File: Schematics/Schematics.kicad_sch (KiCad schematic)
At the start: 19 parts, among them U1 TP4056, U2 BH1750, U3 BME688, U4 BU30TD3WG, U5 NRF52840-DONGLE, U6 LIS3DH

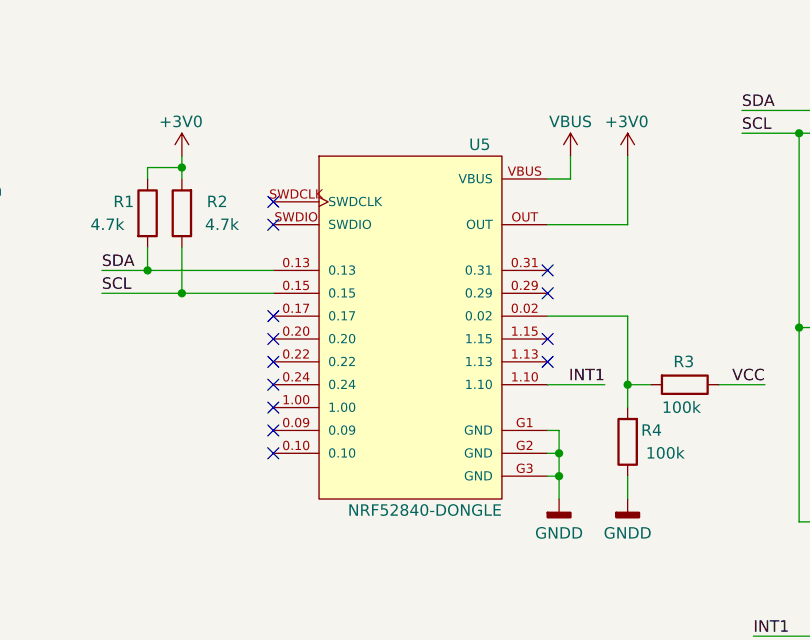
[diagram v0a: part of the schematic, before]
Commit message: Fixed some footprints and made changes on the leader node pcb
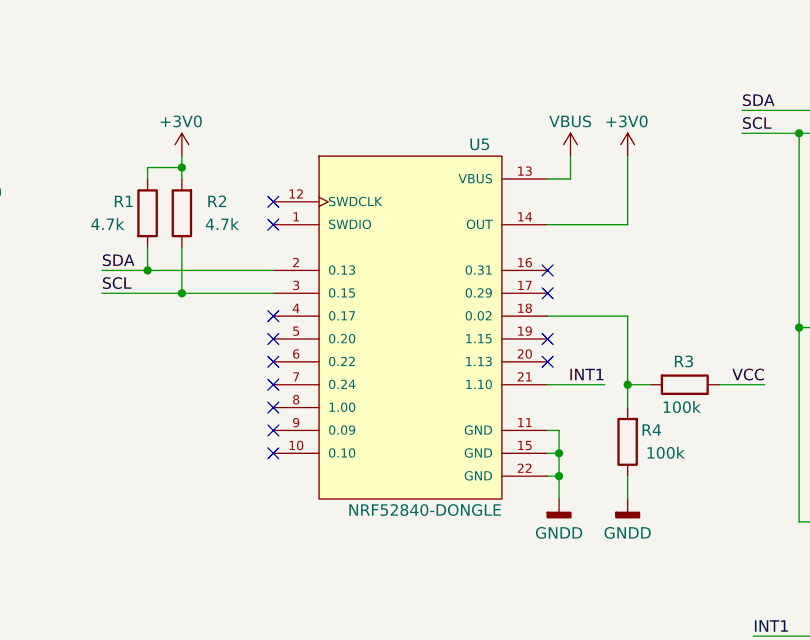
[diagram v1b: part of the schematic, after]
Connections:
- net +3V0: now also U5.14 (OUT); no longer U5.OUT
- net GNDD: now also U5.11 (GND), U5.15 (GND), U5.22 (GND); no longer U5.G1 (GND), U5.G2 (GND), U5.G3 (GND)
- net INT1: now also U5.21 (1.10); no longer U5.1.10
- net SCL: now also U5.3 (0.15); no longer U5.0.15
- net SDA: now also U5.2 (0.13); no longer U5.0.13
- net VBUS: now also U5.13 (VBUS); no longer U5.VBUS
- net at R3.2, R4.2: now also U5.18 (0.02); no longer U5.0.02
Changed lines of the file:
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@@
       (effects (font (size 1.27 1.27)) (justify right))
     )
-    (property "Footprint" "custom:MODULE_NRF52840-DONGLE" (id 2) (at 153.67 88.9 0)
+    (property "Footprint" "custom:MODULE_NRF52840-DONGLE" (id 2) (at 153.67 114.3 0)
       (effects (font (size 1.27 1.27)) (justify bottom) hide)
     )
@@
       (effects (font (size 1.27 1.27)) (justify bottom) hide)
     )
-    (property "STANDARD" "Manufacturer Recommendations" (id 5) (at 154.94 91.44 0)
+    (property "STANDARD" "Manufacturer Recommendations" (id 5) (at 158.75 116.84 0)
       (effects (font (size 1.27 1.27)) (justify bottom) hide)
     )
@@
       (effects (font (size 1.27 1.27)) (justify bottom) hide)
     )
-    (property "MANUFACTURER" "Nordic semiconductor" (id 7) (at 153.67 86.36 0)
+    (property "MANUFACTURER" "Nordic semiconductor" (id 7) (at 152.4 111.76 0)
       (effects (font (size 1.27 1.27)) (justify bottom) hide)
     )
-    (pin "0.02")
-    (pin "0.09")
-    (pin "0.10")
-    (pin "0.13")
-    (pin "0.15")
-    (pin "0.17")
-    (pin "0.20")
-    (pin "0.22")
-    (pin "0.24")
-    (pin "0.29")
-    (pin "0.31")
-    (pin "1.00")
-    (pin "1.10")
-    (pin "1.13")
-    (pin "1.15")
-    (pin "G1")
-    (pin "G2")
-    (pin "G3")
-    (pin "OUT")
-    (pin "SWDCLK")
-    (pin "SWDIO")
-    (pin "VBUS")
+    (pin "12")
+    (pin "9")
+    (pin "10")
+    (pin "11")
+    (pin "13")
+    (pin "14")
+    (pin "15")
+    (pin "16")
+    (pin "17")
+    (pin "18")
+    (pin "19")
+    (pin "1")
+    (pin "20")
+    (pin "21")
+    (pin "22")
+    (pin "2")
+    (pin "3")
+    (pin "4")
+    (pin "5")
+    (pin "6")
+    (pin "7")
+    (pin "8")
   )
   (symbol (lib_id "Device:C") (at 57.15 104.14 0) (unit 1)

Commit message: Changes on the vodesht_vyzel pcb and schematics
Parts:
- removed BT1: 3.7V Li-ion, custom:BHC-18650-1P, symbol Device:Battery
- added BT1: 3.7V Li-ion, custom:BHC-18650-1P, symbol Device:Battery_Cell
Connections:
- net at U1.4 (B+): now also BT1.1 (+)
- net at U1.5 (B-): now also BT1.2 (-)
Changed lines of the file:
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@@
   (no_connect (at 168.91 91.44))
   (no_connect (at 138.43 93.98))
-  (wire (pts (xy 96.52 64.77) (xy 96.52 66.04))
+  (wire (pts (xy 96.52 64.77) (xy 96.52 67.31))
     (stroke (width 0) (type default) (color 0 0 0 0))
   )
@@
     (stroke (width 0) (type default) (color 0 0 0 0))
   )
-  (wire (pts (xy 96.52 77.47) (xy 96.52 76.2))
+  (wire (pts (xy 96.52 74.93) (xy 96.52 77.47))
     (stroke (width 0) (type default) (color 0 0 0 0))
   )
@@
     (pin "9")
   )
+  (symbol (lib_id "Device:Battery_Cell") (at 96.52 72.39 0) (unit 1)
+    (in_bom yes) (on_board yes) (fields_autoplaced)
+    (property "Reference" "BT1" (id 0) (at 100.33 69.0879 0)
+      (effects (font (size 1.27 1.27)) (justify left))
+    )
+    (property "Value" "3.7V Li-ion" (id 1) (at 100.33 71.6279 0)
+      (effects (font (size 1.27 1.27)) (justify left))
+    )
+    (property "Footprint" "custom:BHC-18650-1P" (id 2) (at 96.52 70.866 90)
+      (effects (font (size 1.27 1.27)) hide)
+    )
+    (property "Datasheet" "~" (id 3) (at 96.52 70.866 90)
+      (effects (font (size 1.27 1.27)) hide)
+    )
+    (pin "1")
+    (pin "2")
+  )
   (symbol (lib_id "power:GNDD") (at 59.69 77.47 0) (unit 1)
     (in_bom yes) (on_board yes)
@@
       (effects (font (size 1.27 1.27)) (justify bottom) hide)
     )
-    (pin "12")
-    (pin "9")
+    (pin "1")
     (pin "10")
     (pin "11")
+    (pin "12")
     (pin "13")
     (pin "14")
@@
     (pin "18")
     (pin "19")
-    (pin "1")
+    (pin "2")
     (pin "20")
     (pin "21")
     (pin "22")
-    (pin "2")
     (pin "3")
     (pin "4")
@@
     (pin "7")
     (pin "8")
+    (pin "9")
   )
   (symbol (lib_id "Device:C") (at 57.15 104.14 0) (unit 1)
@@
     )
   )
-  (symbol (lib_id "Device:Battery") (at 96.52 71.12 0) (unit 1)
-    (in_bom yes) (on_board yes)
-    (property "Reference" "BT1" (id 0) (at 100.33 68.58 0)
-      (effects (font (size 1.27 1.27)) (justify left))
-    )
-    (property "Value" "3.7V Li-ion" (id 1) (at 99.06 74.93 0)
-      (effects (font (size 1.27 1.27)) (justify left))
-    )
-    (property "Footprint" "custom:BHC-18650-1P" (id 2) (at 96.52 69.596 90)
-      (effects (font (size 1.27 1.27)) hide)
-    )
-    (property "Datasheet" "~" (id 3) (at 96.52 69.596 90)
-      (effects (font (size 1.27 1.27)) hide)
-    )
-    (pin "1")
-    (pin "2")
-  )
   (symbol (lib_id "power:VCC") (at 57.15 92.71 0) (unit 1)
     (in_bom yes) (on_board yes)
@@
       (reference "#PWR0108") (unit 1) (value "GNDD") (footprint "")
     )
-    (path "/dda09fab-e2de-4513-91bf-ba56c5a416f3"
+    (path "/1582a466-2330-4b44-a78b-0c25434ba44a"
       (reference "BT1") (unit 1) (value "3.7V Li-ion") (footprint "custom:BHC-18650-1P")
     )
